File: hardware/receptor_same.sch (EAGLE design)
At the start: 1 part, among them U1 ATMEGA328P_TQFP

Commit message: avances mcu
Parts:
- added C1, C2: 0.1uF, OPL_Capacitor:CERAMIC-100NF-50V-10%-X7R(0603)
- added Y1: 8MHz, SparkFun-Clocks:RESONATOR-8MHZSMD_3.2X1.3
- U1: MPN (none) -> ATMEGA328P-AU
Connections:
- new net GND: C1.1, C2.2, U1.AGND, U1.GND@3, U1.GND@5, Y1.2
- new net N$1: U1.PB6(XTAL1/TOSC1), Y1.1
- new net N$2: U1.PB7(XTAL2/TOSC2), Y1.3
- new net N$3: C1.2, U1.AREF
- new net VCC: C2.1, U1.AVCC, U1.VCC@4, U1.VCC@6

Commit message: icsp
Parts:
- added J1: ICSP, OPL_Connector:DIP-BLACK-MALE-HEADER(2X3P-2.54）-2.54
- added R1: 10k, OPL_Resistor:SMD-RES-10K-5%-1/10W(0603)
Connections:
- new net N$4: J1.1, U1.PB4(MISO)
- new net N$5: J1.3, U1.PB5(SCK)
- new net N$6: J1.4, U1.PB3(MOSI/OC2)
- new net RST: J1.5, R1.1, U1.PC6(/RESET)
- net GND: now also J1.6
- net VCC: now also J1.2, R1.2
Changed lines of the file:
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@@
 <?xml version="1.0" encoding="utf-8"?>
 <!DOCTYPE eagle SYSTEM "eagle.dtd">
-<eagle version="9.3.2">
+<eagle version="9.4.0">
 <drawing>
 <settings>
@@
 <part name="GND3" library="supply1" library_urn="urn:adsk.eagle:library:371" deviceset="GND" device=""/>
 <part name="P+2" library="supply1" library_urn="urn:adsk.eagle:library:371" deviceset="VCC" device=""/>
+<part name="J1" library="OPL_Connector" library_urn="urn:adsk.eagle:library:8004395" deviceset="DIP-BLACK-MALE-HEADER(2X3P-2.54）" device="-2.54" package3d_urn="urn:adsk.eagle:package:8004534/1" value="ICSP"/>
+<part name="GND4" library="supply1" library_urn="urn:adsk.eagle:library:371" deviceset="GND" device=""/>
+<part name="P+3" library="supply1" library_urn="urn:adsk.eagle:library:371" deviceset="VCC" device=""/>
+<part name="R1" library="OPL_Resistor" library_urn="urn:adsk.eagle:library:8004883" deviceset="SMD-RES-10K-5%-1/10W(0603)" device="" package3d_urn="urn:adsk.eagle:package:8004941/1" value="10k"/>
+<part name="P+4" library="supply1" library_urn="urn:adsk.eagle:library:371" deviceset="VCC" device=""/>
 </parts>
 <sheets>
@@
 <attribute name="VALUE" x="153.67" y="137.16" size="1.27" layer="96" ratio="10"/>
 </instance>
-<instance part="P+1" gate="VCC" x="160.02" y="165.1" smashed="yes">
-<attribute name="VALUE" x="160.02" y="167.64" size="1.778" layer="96" rot="R180"/>
+<instance part="P+1" gate="VCC" x="144.78" y="157.48" smashed="yes">
+<attribute name="VALUE" x="144.78" y="160.02" size="1.778" layer="96" rot="R180"/>
 </instance>
 <instance part="GND2" gate="1" x="160.02" y="88.9" smashed="yes">
@@
 <instance part="P+2" gate="VCC" x="147.32" y="106.68" smashed="yes">
 <attribute name="VALUE" x="147.32" y="109.22" size="1.778" layer="96" rot="R180"/>
+</instance>
+<instance part="J1" gate="J" x="231.14" y="78.74" smashed="yes">
+<attribute name="NAME" x="224.79" y="85.09" size="1.27" layer="95" ratio="10"/>
+<attribute name="VALUE" x="231.14" y="85.09" size="1.27" layer="96" ratio="10"/>
+</instance>
+<instance part="GND4" gate="1" x="241.3" y="86.36" smashed="yes" rot="R180">
+<attribute name="VALUE" x="243.84" y="88.9" size="1.778" layer="96" rot="R180"/>
+</instance>
+<instance part="P+3" gate="VCC" x="215.9" y="86.36" smashed="yes">
+<attribute name="VALUE" x="215.9" y="88.9" size="1.778" layer="96" rot="R180"/>
+</instance>
+<instance part="R1" gate="G$1" x="160.02" y="160.02" smashed="yes" rot="R90">
+<attribute name="NAME" x="158.75" y="161.29" size="1.27" layer="95" ratio="10" rot="R180"/>
+<attribute name="VALUE" x="165.1" y="160.02" size="1.27" layer="96" ratio="10" rot="R180"/>
+</instance>
+<instance part="P+4" gate="VCC" x="160.02" y="167.64" smashed="yes">
+<attribute name="VALUE" x="160.02" y="170.18" size="1.778" layer="96" rot="R180"/>
 </instance>
 </instances>
@@
 <wire x1="147.32" y1="92.71" x2="147.32" y2="91.44" width="0.1524" layer="91"/>
 </segment>
+<segment>
+<pinref part="J1" gate="J" pin="6"/>
+<wire x1="240.03" y1="81.28" x2="241.3" y2="81.28" width="0.1524" layer="91"/>
+<pinref part="GND4" gate="1" pin="GND"/>
+<wire x1="241.3" y1="81.28" x2="241.3" y2="83.82" width="0.1524" layer="91"/>
+</segment>
 </net>
 <net name="N$3" class="0">
@@
 <pinref part="U1" gate="U$1" pin="VCC@6"/>
 <pinref part="P+1" gate="VCC" pin="VCC"/>
-<wire x1="162.56" y1="144.78" x2="160.02" y2="144.78" width="0.1524" layer="91"/>
-<wire x1="160.02" y1="144.78" x2="160.02" y2="147.32" width="0.1524" layer="91"/>
+<wire x1="162.56" y1="144.78" x2="144.78" y2="144.78" width="0.1524" layer="91"/>
+<wire x1="144.78" y1="144.78" x2="144.78" y2="147.32" width="0.1524" layer="91"/>
 <pinref part="U1" gate="U$1" pin="VCC@4"/>
-<wire x1="160.02" y1="147.32" x2="160.02" y2="149.86" width="0.1524" layer="91"/>
-<wire x1="160.02" y1="149.86" x2="160.02" y2="162.56" width="0.1524" layer="91"/>
-<wire x1="162.56" y1="147.32" x2="160.02" y2="147.32" width="0.1524" layer="91"/>
-<junction x="160.02" y="147.32"/>
+<wire x1="144.78" y1="147.32" x2="144.78" y2="149.86" width="0.1524" layer="91"/>
+<wire x1="144.78" y1="149.86" x2="144.78" y2="154.94" width="0.1524" layer="91"/>
+<wire x1="162.56" y1="147.32" x2="144.78" y2="147.32" width="0.1524" layer="91"/>
+<junction x="144.78" y="147.32"/>
 <pinref part="U1" gate="U$1" pin="AVCC"/>
-<wire x1="162.56" y1="149.86" x2="160.02" y2="149.86" width="0.1524" layer="91"/>
-<junction x="160.02" y="149.86"/>
+<wire x1="162.56" y1="149.86" x2="144.78" y2="149.86" width="0.1524" layer="91"/>
+<junction x="144.78" y="149.86"/>
 </segment>
 <segment>
@@
 <wire x1="147.32" y1="104.14" x2="147.32" y2="100.33" width="0.1524" layer="91"/>
 </segment>
-</net>
+<segment>
+<pinref part="J1" gate="J" pin="2"/>
+<wire x1="222.25" y1="78.74" x2="215.9" y2="78.74" width="0.1524" layer="91"/>
+<pinref part="P+3" gate="VCC" pin="VCC"/>
+<wire x1="215.9" y1="78.74" x2="215.9" y2="83.82" width="0.1524" layer="91"/>
+</segment>
+<segment>
+<pinref part="P+4" gate="VCC" pin="VCC"/>
+<pinref part="R1" gate="G$1" pin="2"/>
+<wire x1="160.02" y1="165.1" x2="160.02" y2="163.83" width="0.1524" layer="91"/>
+</segment>
+</net>
+<net name="N$4" class="0">
+<segment>
+<pinref part="U1" gate="U$1" pin="PB4(MISO)"/>
+<wire x1="210.82" y1="99.06" x2="220.98" y2="99.06" width="0.1524" layer="91"/>
+<wire x1="220.98" y1="99.06" x2="220.98" y2="81.28" width="0.1524" layer="91"/>
+<pinref part="J1" gate="J" pin="1"/>
+<wire x1="220.98" y1="81.28" x2="222.25" y2="81.28" width="0.1524" layer="91"/>
+</segment>
+</net>
+<net name="N$5" class="0">
+<segment>
+<pinref part="U1" gate="U$1" pin="PB5(SCK)"/>
+<wire x1="210.82" y1="96.52" x2="218.44" y2="96.52" width="0.1524" layer="91"/>
+<wire x1="218.44" y1="96.52" x2="218.44" y2="76.2" width="0.1524" layer="91"/>
+<pinref part="J1" gate="J" pin="3"/>
+<wire x1="218.44" y1="76.2" x2="222.25" y2="76.2" width="0.1524" layer="91"/>
+</segment>
+</net>
+<net name="N$6" class="0">
+<segment>
+<pinref part="U1" gate="U$1" pin="PB3(MOSI/OC2)"/>
+<wire x1="210.82" y1="101.6" x2="251.46" y2="101.6" width="0.1524" layer="91"/>
+<wire x1="251.46" y1="101.6" x2="251.46" y2="76.2" width="0.1524" layer="91"/>
+<pinref part="J1" gate="J" pin="4"/>
+<wire x1="251.46" y1="76.2" x2="240.03" y2="76.2" width="0.1524" layer="91"/>
+</segment>
+</net>
+<net name="RST" class="0">
+<segment>
+<pinref part="J1" gate="J" pin="5"/>
+<wire x1="240.03" y1="78.74" x2="241.3" y2="78.74" width="0.1524" layer="91"/>
+<label x="241.3" y="78.74" size="1.778" layer="95" xref="yes"/>
+</segment>
+<segment>
+<pinref part="U1" gate="U$1" pin="PC6(/RESET)"/>
+<wire x1="162.56" y1="154.94" x2="160.02" y2="154.94" width="0.1524" layer="91"/>
+<pinref part="R1" gate="G$1" pin="1"/>
+<wire x1="160.02" y1="154.94" x2="160.02" y2="156.21" width="0.1524" layer="91"/>
+<wire x1="160.02" y1="154.94" x2="157.48" y2="154.94" width="0.1524" layer="91"/>
+<junction x="160.02" y="154.94"/>
+<label x="157.48" y="154.94" size="1.778" layer="95" rot="R180" xref="yes"/>
+</segment>
+</net>

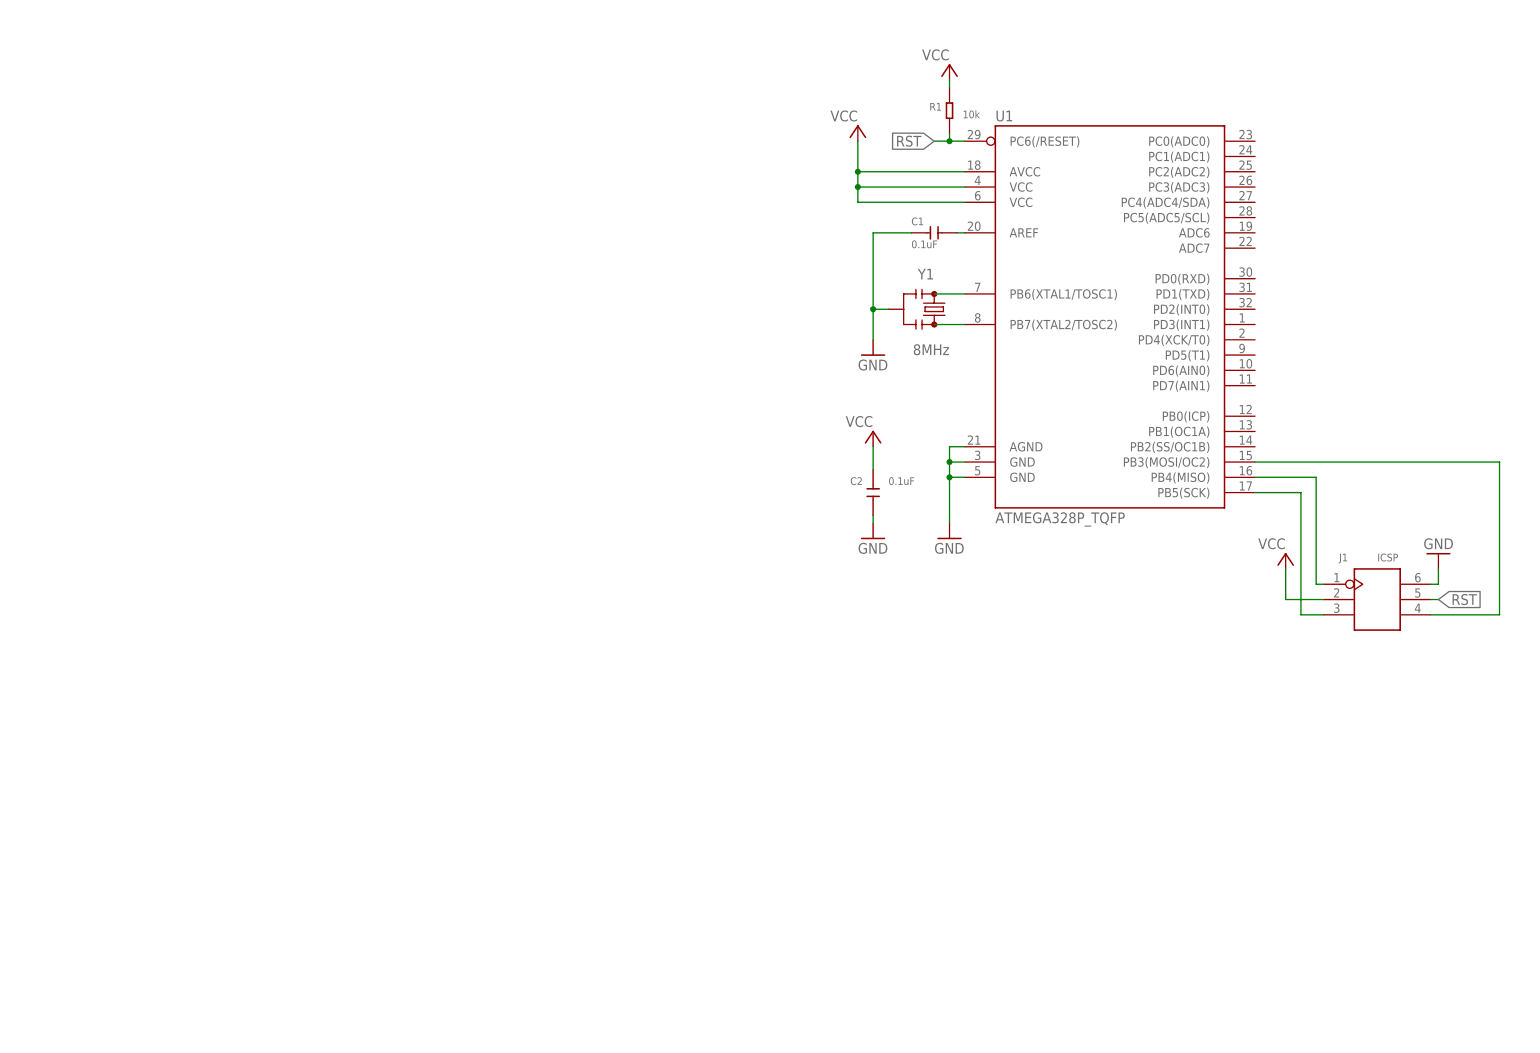
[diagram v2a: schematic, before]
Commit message: separamos icsp
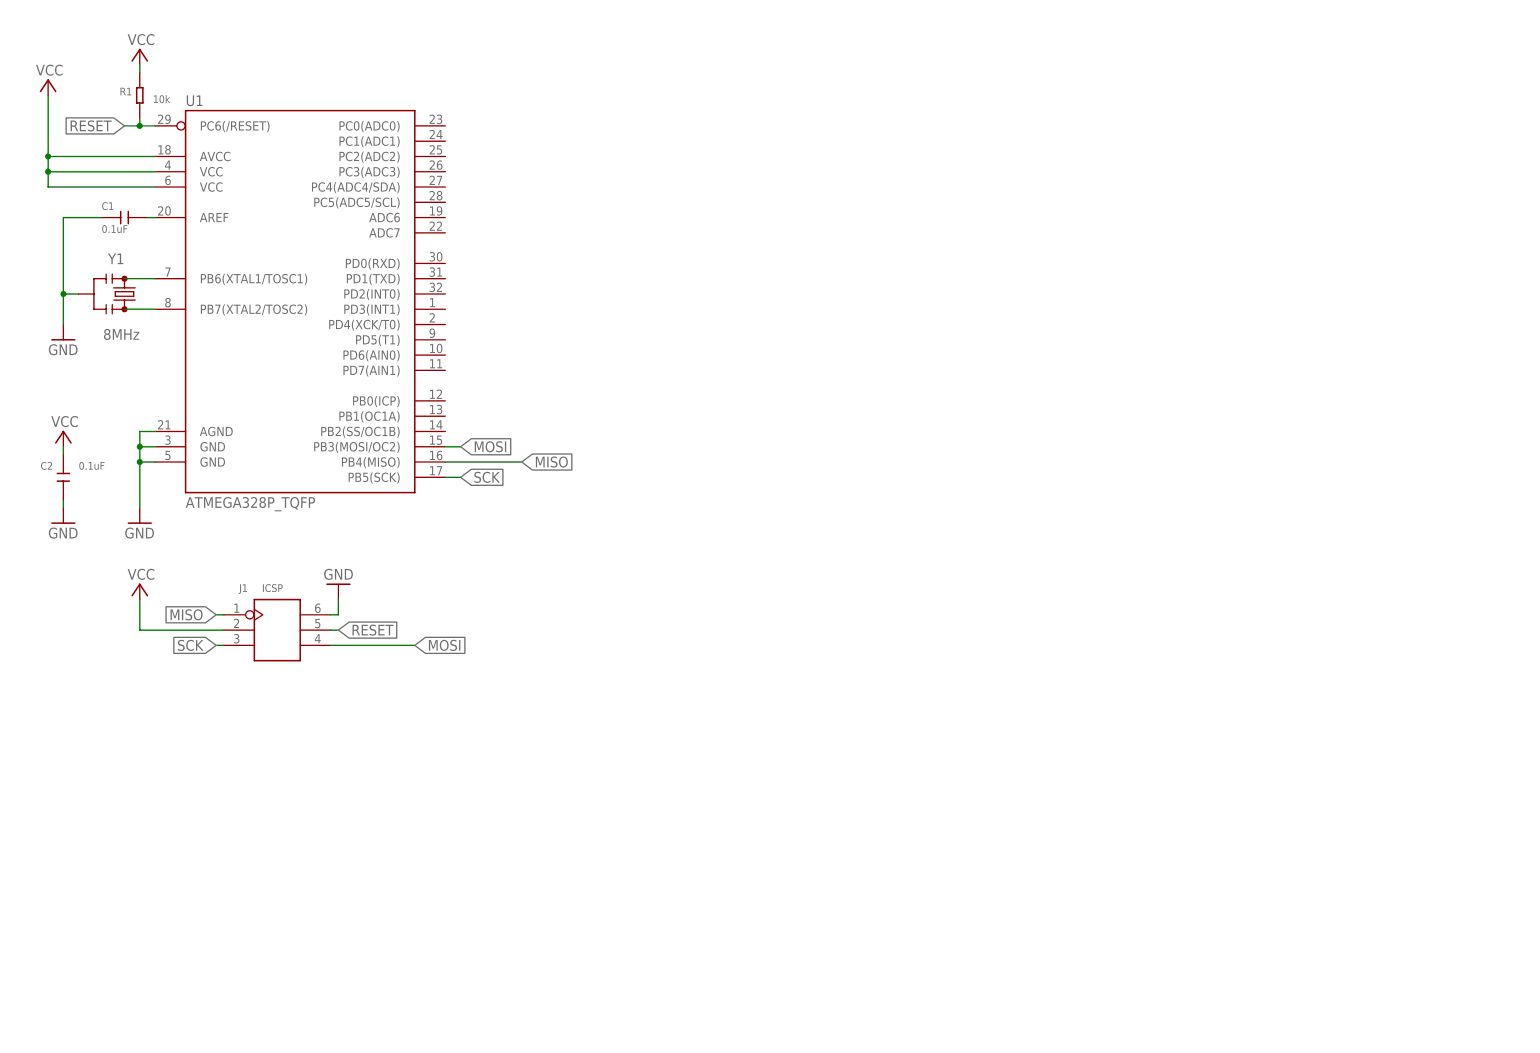
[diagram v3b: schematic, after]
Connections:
- net N$4 renamed MISO
- net N$5 renamed SCK
- net N$6 renamed MOSI
- net RST renamed RESET
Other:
- moved on the sheet: C1, C2, J1, R1, U1, Y1

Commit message: avances si4707 y conctor puerto serial
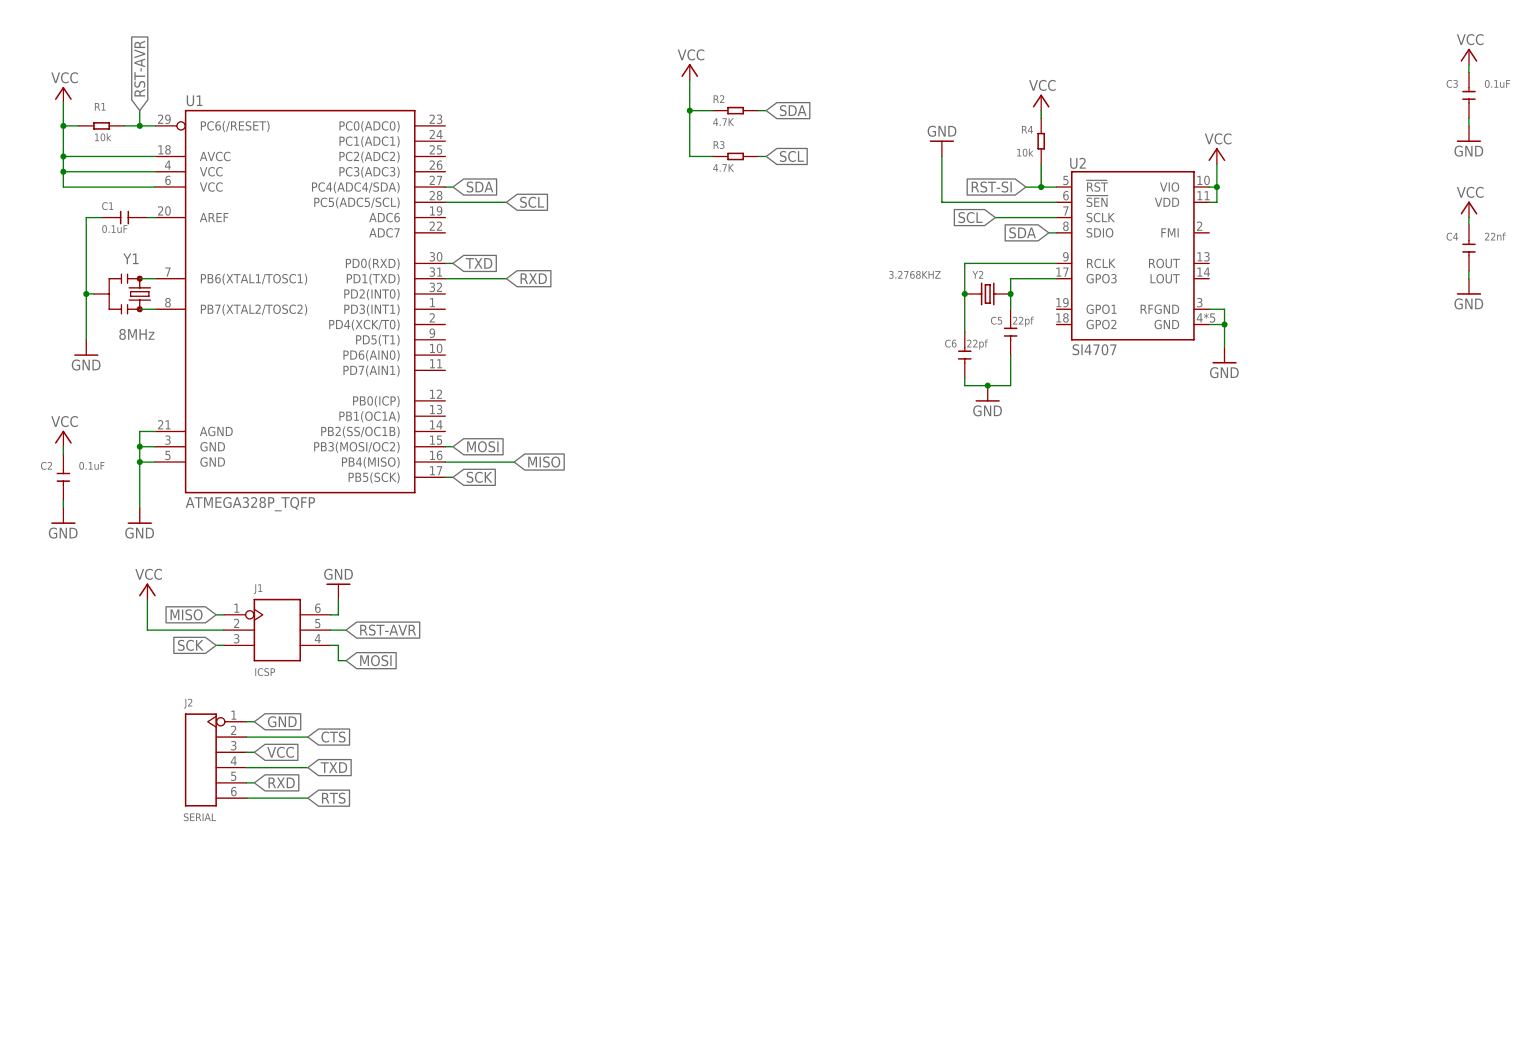
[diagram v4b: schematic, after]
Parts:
- added C3: 0.1uF, OPL_Capacitor:CERAMIC-100NF-50V-10%-X7R(0603)
- added C4: 22nf, OPL_Capacitor:CERAMIC-22NF-50V-10%-X7R(0603)
- added C5, C6: 22pf, OPL_Capacitor:CERAMIC-22PF-50V-5%-NPO(0603)
- added J2: SERIAL, OPL_Connector:DIP-BLACK-MALE-HEADER(6P-2.54)
- added R2, R3: 4.7K, OPL_Resistor:SMD-RES-4.7K-5%-1/10W(0603)
- added R4: 10k, OPL_Resistor:SMD-RES-10K-5%-1/10W(0603)
- added U2: SI4707, si4707:SPARKFUN-RF_SI4707
- added Y2: 3.2768KHZ, OPL_Crystal Oscillator:SMD-CRYSTAL-32.768KHZ-12.5PF-20PPM-90K(2P-L2.0X1.2MM)
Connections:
- net RESET renamed RST-AVR
- new net CTS: J2.2
- new net N$4: C5.2, U2.GPO3, Y2.2
- new net N$5: C6.2, U2.RCLK, Y2.1
- new net RST-SI: R4.2, U2.!RST
- new net RTS: J2.6
- new net RXD: J2.5, U1.PD1(TXD)
- new net SCL: R3.2, U1.PC5(ADC5/SCL), U2.SCLK
- new net SDA: R2.2, U1.PC4(ADC4/SDA), U2.SDIO
- new net TXD: J2.4, U1.PD0(RXD)
- net GND: now also C3.2, C4.2, C5.1, C6.1, J2.1, U2.!SEN, U2.GND, U2.RFGND
- net VCC: now also C3.1, C4.1, J2.3, R2.1, R3.1, R4.1, U2.VDD, U2.VIO
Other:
- moved on the sheet: R1, Y1
